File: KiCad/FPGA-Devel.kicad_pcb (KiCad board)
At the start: 4 copper layers, 100 x 80 mm, 236 parts, among them J401 Conn_02x06_Top_Bottom, J402 Conn_02x06_Top_Bottom, J403 Conn_02x06_Top_Bottom, J404 USB_C_Receptacle_USB2.0_16P, J405 Conn_01x02_Pin, J801 USB_C_Receptacle_USB2.0_16P, Q201 BC847W, Q401 BC857W, Q402 BC857W, Q403 BC857W, Q404 BC857W, Q405 BC857W, SW401 SW_DIP_x04, SW402 SW_DIP_x04, SW403 SW_Omron_B3FS, SW404 SW_Omron_B3FS, SW405 SW_Omron_B3FS, SW406 SW_Omron_B3FS, SW407 SW_Omron_B3FS, SW408 SW_Omron_B3FS, SW409 SW_Omron_B3FS, SW410 SW_Omron_B3FS, SW411 SW_Omron_B3FS, SW412 RotaryEncoder_Switch, SW501 SW_Omron_B3FS, U1001 IS25LP032D-JNLE, U1002 APS6404, U201 TLV62568DDC, U202 TLV62568DDC, U203 TLV62568DDC, U401 LTC-4627JR, U502 XC7S50FTGB196, U801 FT2232HQ, U802 93LCxxB, U901 AP331, U902 74LVC2G53, X401 100MHz, Y801 12MHz

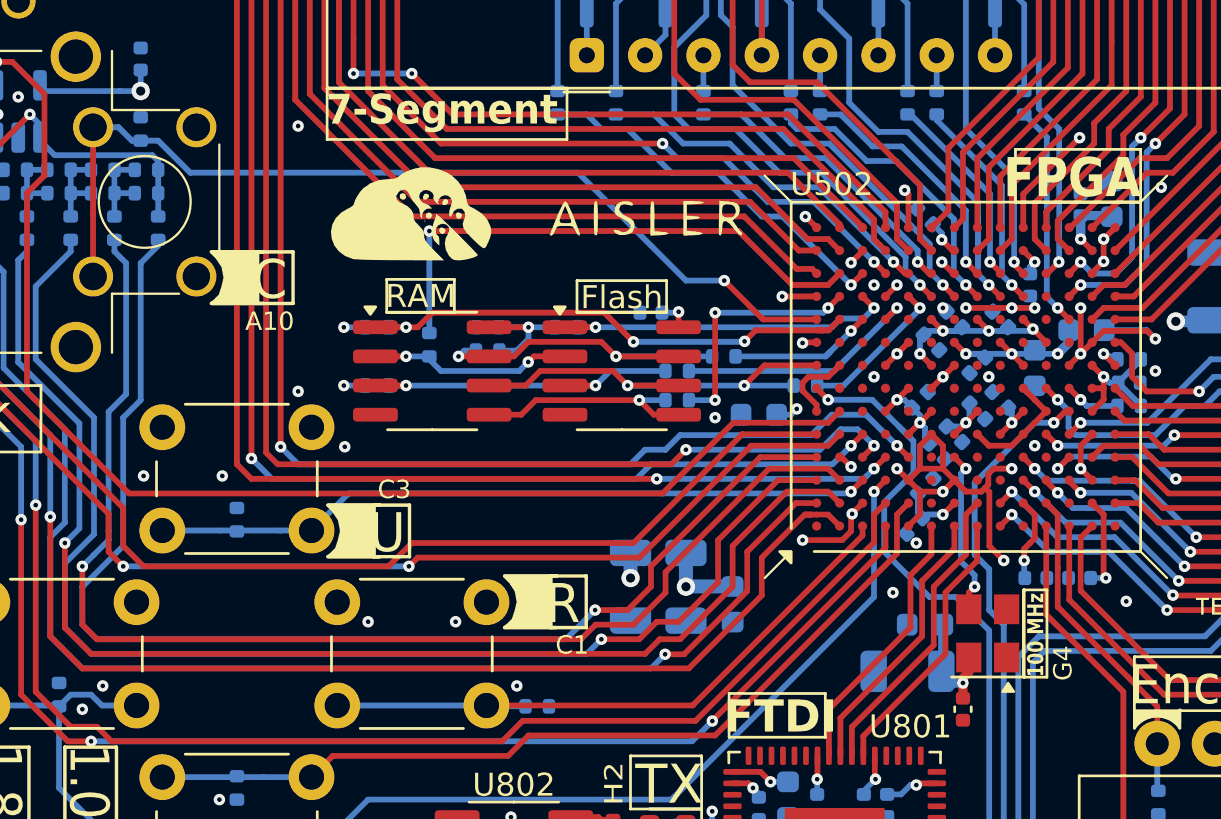
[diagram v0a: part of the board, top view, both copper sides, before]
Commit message: Combo-Footprint für Flash
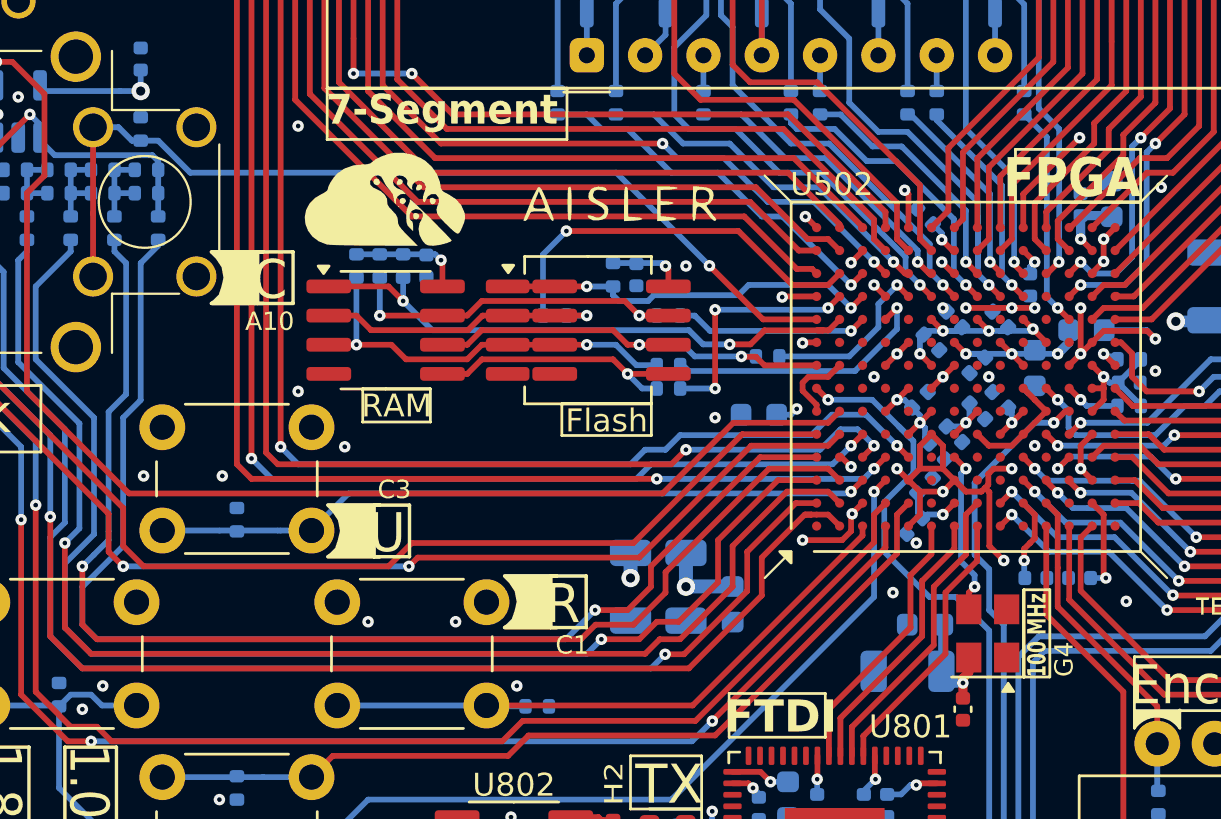
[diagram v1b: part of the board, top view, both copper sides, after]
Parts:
- SW413: value ~ -> RKJXV1224
- U1001: footprint Package_SO:SOIC-8_3.9x4.9mm_P1.27mm -> Library:SOIC-8_4_5.3_combo_P1.27mm
- moved R1001 5.97 mm to (71.0, 96.8), turned to 90 degrees
- moved R604 5.61 mm to (78.6, 98.9), turned to 180 degrees
- moved R1002 5.28 mm to (70.0, 96.8), turned to 90 degrees
- moved C1002 3.77 mm to (73.0, 96.8), turned to -90 degrees
- moved R1003 3.06 mm to (81.2, 97.2), turned to -90 degrees
- moved R606 3.00 mm to (83.6, 98.9)
- moved R601 2.90 mm to (72.0, 96.8), turned to 90 degrees
- moved U1002 2.70 mm to (71.2, 99.6)
- moved R602 2.08 mm to (87.9, 100.7)
- moved U1001 1.83 mm to (81.1, 99.6)
- moved C1001 1.77 mm to (82.2, 97.2), turned to -90 degrees
- moved G*** 1.31 mm to (76.7, 93.9)
- moved R603 0.63 mm to (83.6, 102.1)
- moved R605 0.46 mm to (83.6, 101.1)
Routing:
- net Net-(U502A-IO_L1N_T0_D01_DIN_14): track 23.5 -> 17.2 mm
- net /Memory/SPI_Mem.MISO: track 8.02 -> 13.5 mm, vias 2 -> 1
- net /Memory/SPI_Mem.MOSI: track 9.16 -> 11.9 mm
- net /Memory/SPI_Mem.CS1: track 22.9 -> 25.5 mm, vias 3 -> 2
- net /Memory/SPI_Mem.WP: track 15.8 -> 18.1 mm
- net Net-(U502A-IO_L2N_T0_D03_14): track 6.48 -> 8.43 mm
- net /Memory/SPI_Mem.HOLD: track 14.4 -> 16.3 mm
- net +3.3V: track 93.0 -> 91.2 mm, vias 37 -> 35
- net Net-(U502A-IO_0_14): track 6.61 -> 7.73 mm
- net Net-(U502A-IO_L2P_T0_D02_14): track 11.0 -> 11.9 mm
- net /Memory/SPI_Mem.CS0: track 16.0 -> 16.9 mm

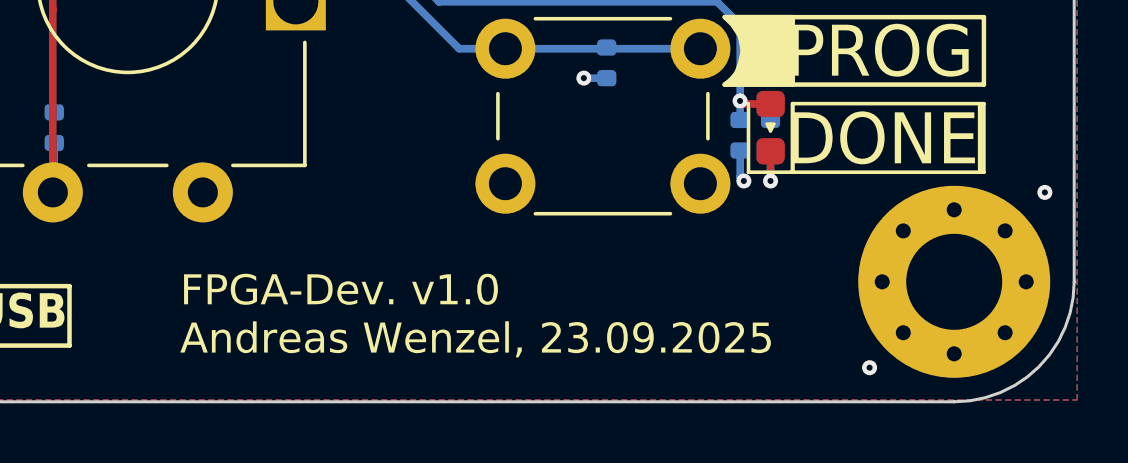
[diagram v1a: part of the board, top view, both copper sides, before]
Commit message: Combo-Footprint für Flash (auch im Schematic)
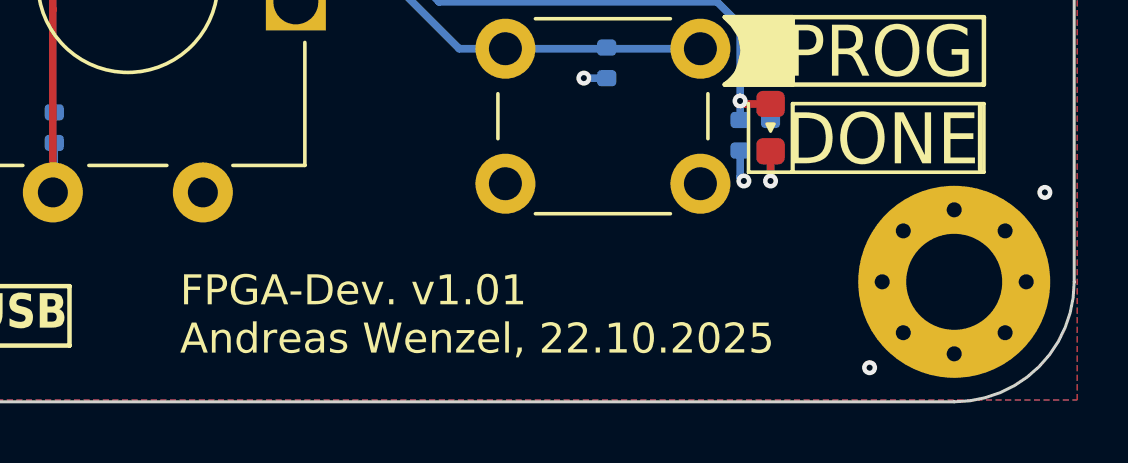
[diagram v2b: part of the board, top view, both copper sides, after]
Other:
- board text added: "FPGA-Dev. v1.01 Andreas Wenzel, 22.10.2025"
- board text removed: "FPGA-Dev. v1.0 Andreas Wenzel, 23.09.2025"
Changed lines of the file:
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@@
 		)
 	)
-	(gr_text "FPGA-Dev. v1.0\nAndreas Wenzel, 23.09.2025"
+	(gr_text "FPGA-Dev. v1.01\nAndreas Wenzel, 22.10.2025"
 		(at 109.093 137.541 0)
 		(layer "F.SilkS")

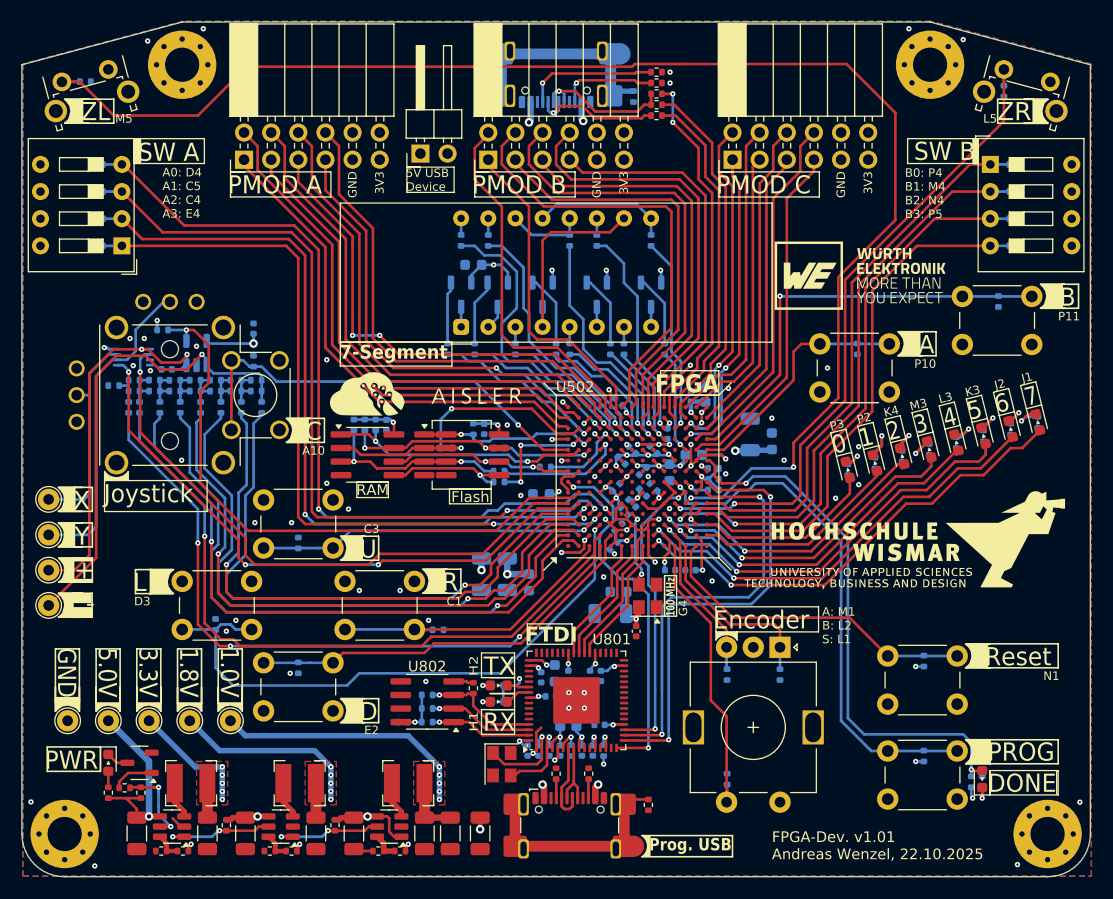
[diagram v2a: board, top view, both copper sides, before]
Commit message: kleine Layout-Anpassungen, Silkscreen korrigiert
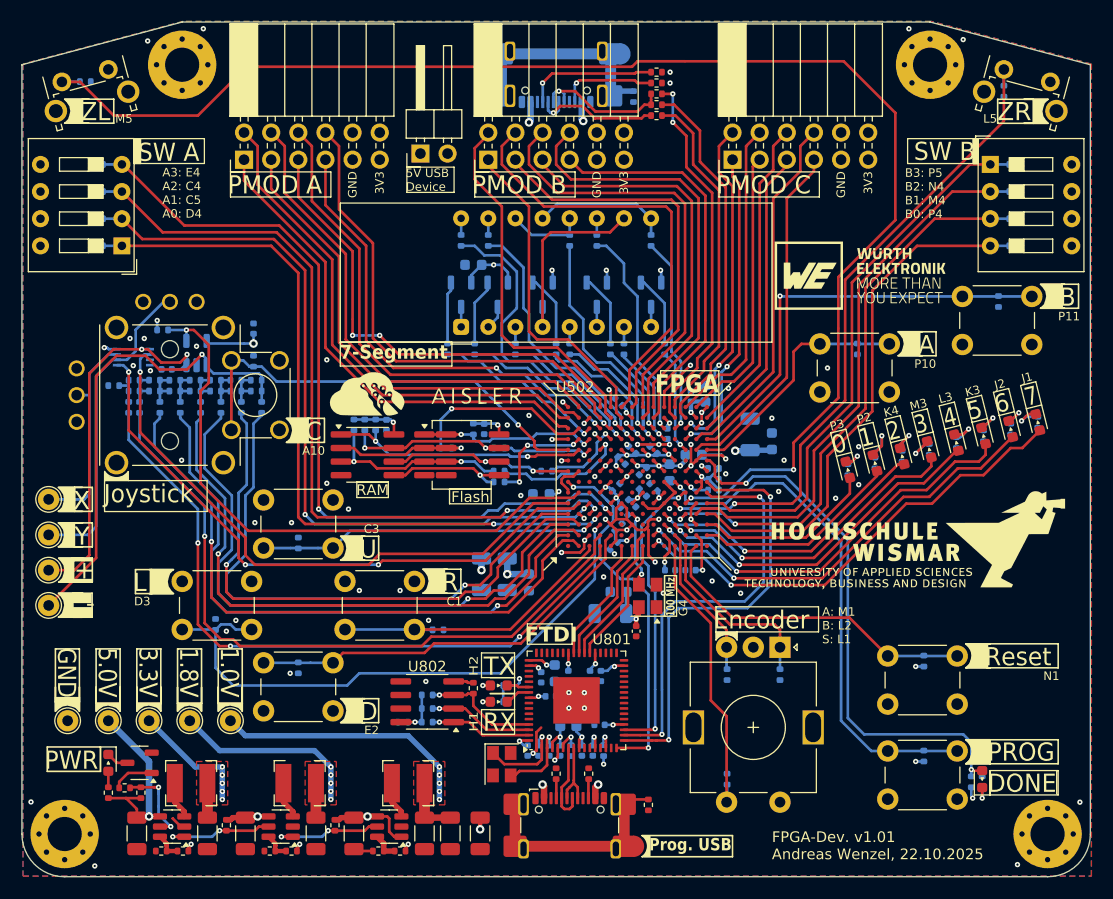
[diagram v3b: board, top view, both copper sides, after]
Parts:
- moved R602 0.40 mm to (88.0, 101.1)
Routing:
- net /IO/SW.A3: track 77.1 -> 76.3 mm
- net /IO/SW.A2: track 74.5 -> 73.7 mm
- net /IO/SW.A1: track 72.7 -> 71.9 mm
- net /IO/SW.A0: track 71.9 -> 71.1 mm
- net /Memory/SPI_Mem.CS1: track 25.5 -> 24.9 mm
- net GND: vias 76 -> 80
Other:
- board text added: "A3: E4 A2: C4 A1: C5 A0: D4"
- board text added: "B3: P5 B2: N4 B1: M4 B0: P4"
- board text removed: "A0: D4 A1: C5 A2: C4 A3: E4"
- board text removed: "B0: P4 B1: M4 B2: N4 B3: P5"
